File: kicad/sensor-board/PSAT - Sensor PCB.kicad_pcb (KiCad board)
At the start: 2 copper layers, 120 x 120 mm, 16 parts, among them J1 MCU Conn_01x04, J2 Conn_01x02, J3 Conn_01x03, J4 Conn_01x03, J5 Conn_01x01, U1 MPU-6000, U2 BME280

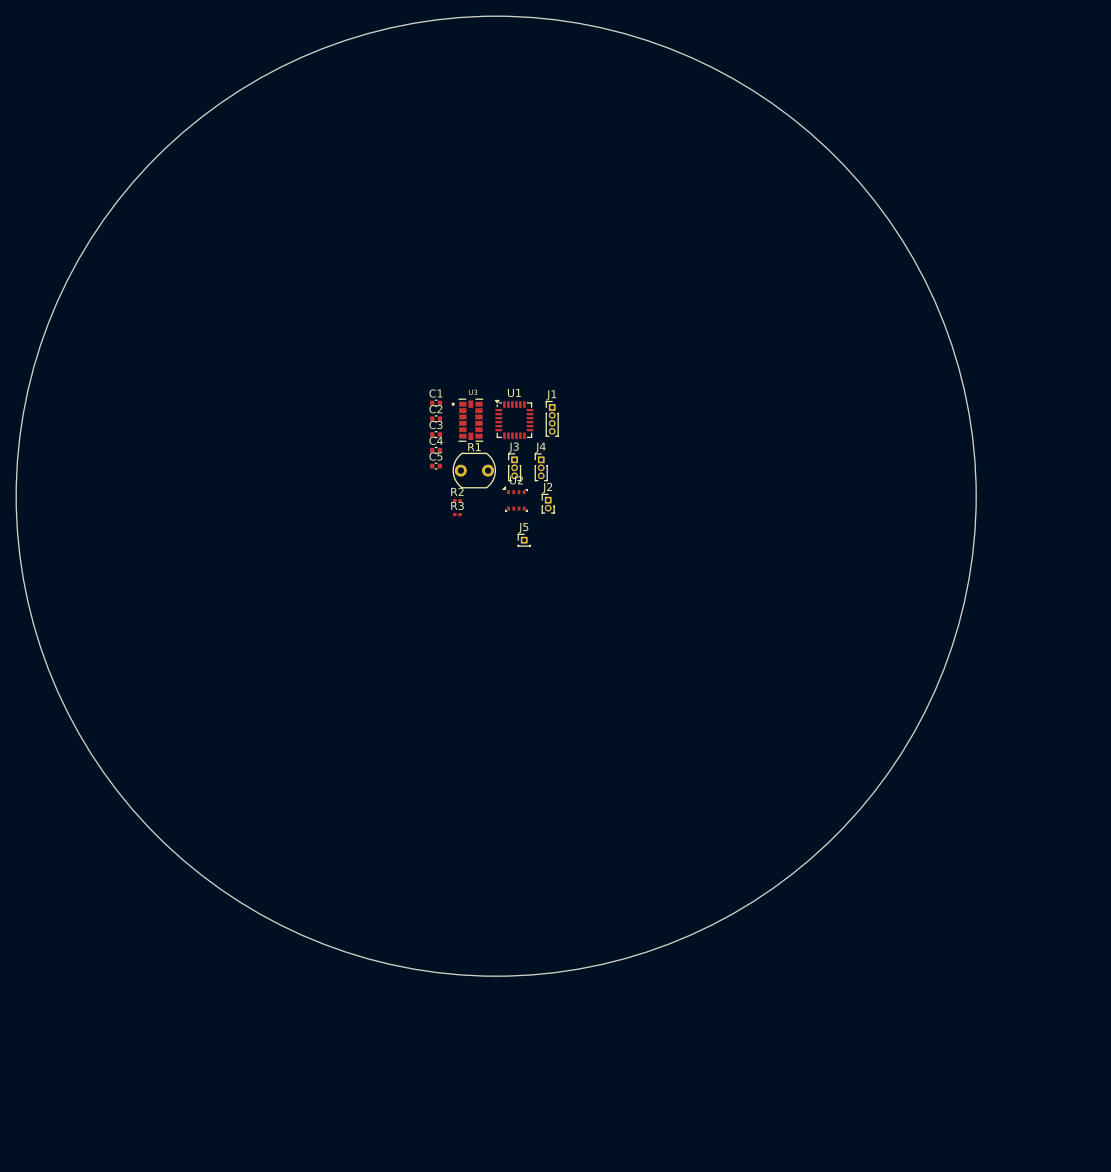
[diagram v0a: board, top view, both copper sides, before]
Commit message: feat: sensor board schematic and started pcb
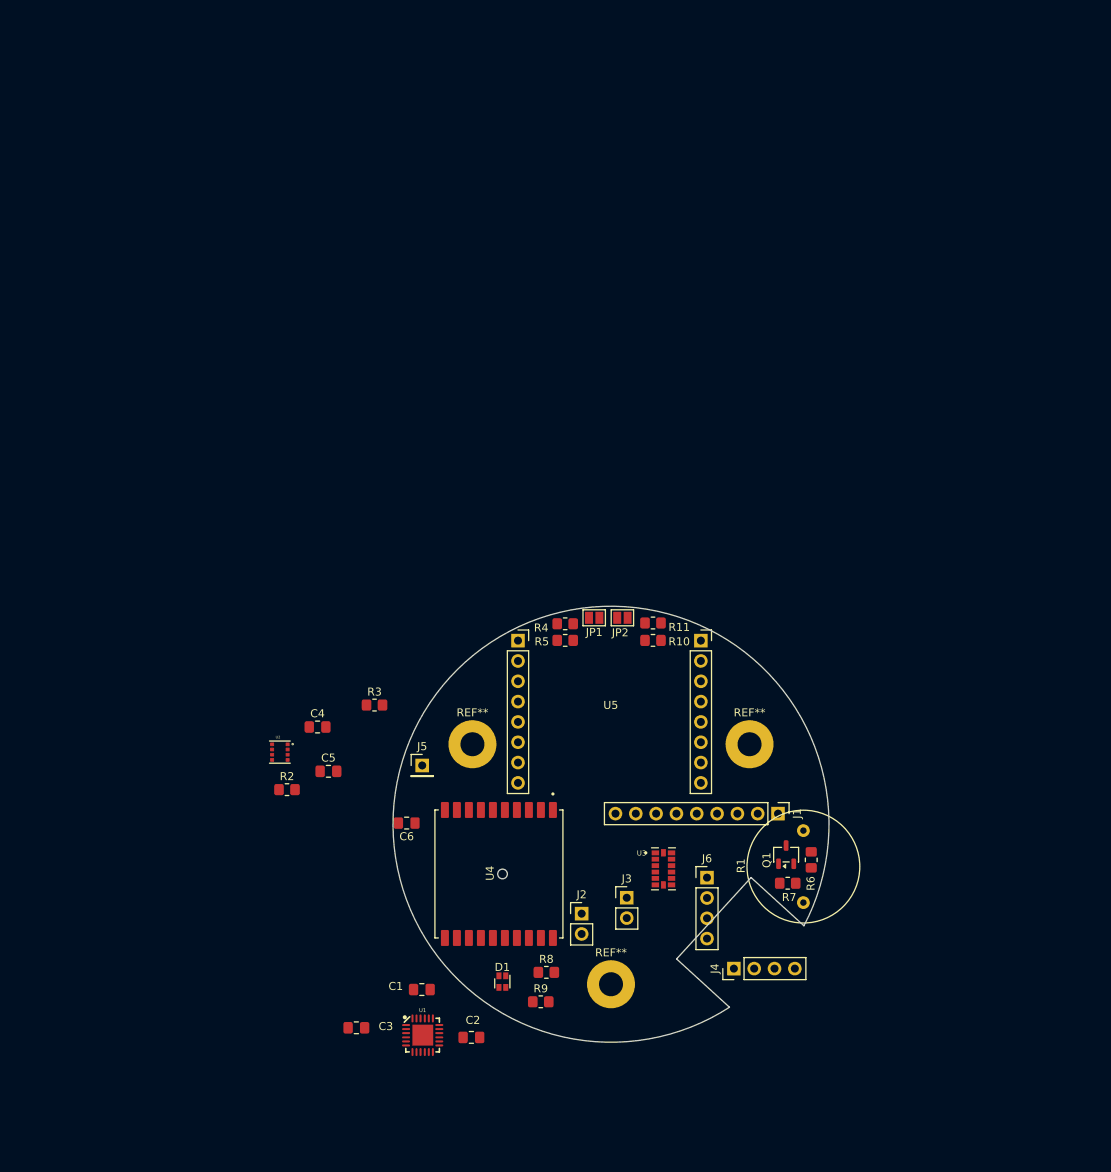
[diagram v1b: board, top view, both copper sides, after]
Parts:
- added C6: 22uF, Capacitor_SMD:C_0805_2012Metric_Pad1.18x1.45mm_HandSolder, F.Cu at (92.3, 140.4)
- added D1: LED, LED_SMD:LED_LiteOn_LTST-C19HE1WT, F.Cu at (104.3, 160.2)
- added J6: MCU - Conn_01x04, Connector_PinHeader_2.54mm:PinHeader_1x04_P2.54mm_Vertical, F.Cu at (129.8, 147.2)
- added JP1: EN_5, Jumper:SolderJumper-2_P1.3mm_Open_Pad1.0x1.5mm, F.Cu at (115.8, 114.7)
- added JP2: EN_5, Jumper:SolderJumper-2_P1.3mm_Open_Pad1.0x1.5mm, F.Cu at (119.3, 114.7)
- added Q1: Q_NPN_BCE, Package_TO_SOT_SMD:SOT-23-3, F.Cu at (139.7, 144.3)
- added R10: 1k5, Resistor_SMD:R_0805_2012Metric_Pad1.20x1.40mm_HandSolder, F.Cu at (123.1, 117.5)
- added R11: 1Meg, Resistor_SMD:R_0805_2012Metric_Pad1.20x1.40mm_HandSolder, F.Cu at (123.1, 115.3)
- added R4: 1k5, Resistor_SMD:R_0805_2012Metric_Pad1.20x1.40mm_HandSolder, F.Cu at (112.1, 115.5)
- added R5: 1Meg, Resistor_SMD:R_0805_2012Metric_Pad1.20x1.40mm_HandSolder, F.Cu at (112.1, 117.5)
- added R6: 10k, Resistor_SMD:R_0805_2012Metric_Pad1.20x1.40mm_HandSolder, F.Cu at (142.9, 145.0)
- added R7: 10k, Resistor_SMD:R_0805_2012Metric_Pad1.20x1.40mm_HandSolder, F.Cu at (139.9, 147.9)
- added R8: 1k, Resistor_SMD:R_0805_2012Metric_Pad1.20x1.40mm_HandSolder, F.Cu at (109.8, 159.0)
- added R9: 180k, Resistor_SMD:R_0805_2012Metric_Pad1.20x1.40mm_HandSolder, F.Cu at (109.1, 162.7)
- added REF**: MountingHole_3mm_Pad, MountingHole:MountingHole_3mm_Pad, F.Cu at (100.5, 130.5)
- added REF**: MountingHole_3mm_Pad, MountingHole:MountingHole_3mm_Pad, F.Cu at (117.9, 160.5)
- added REF**: MountingHole_3mm_Pad, MountingHole:MountingHole_3mm_Pad, F.Cu at (135.2, 130.5)
- added U4: CD-PA1616D, gps:XCVR_CD-PA1616D, F.Cu at (103.8, 146.7)
- added U5: ESP32-CAM, Connector_PinSocket_2.54mm:ESPCam, F.Cu at (117.8, 126.1)
- C1, C2, C3, C4, C5: footprint Capacitor_SMD:C_0402_1005Metric -> Capacitor_SMD:C_0805_2012Metric_Pad1.18x1.45mm_HandSolder
- J1: value MCU Conn_01x04 -> Conn_01x09_Pin; footprint Connector_PinHeader_1.00mm:PinHeader_1x04_P1.00mm_Vertical -> Connector_PinHeader_2.54mm:PinHeader_1x09_P2.54mm_Vertical
- J2: footprint Connector_PinHeader_1.00mm:PinHeader_1x02_P1.00mm_Vertical -> Connector_PinHeader_2.54mm:PinHeader_1x02_P2.54mm_Vertical
- J3: value Conn_01x03 -> MCU - Conn_01x02; footprint Connector_PinHeader_1.00mm:PinHeader_1x03_P1.00mm_Vertical -> Connector_PinHeader_2.54mm:PinHeader_1x02_P2.54mm_Vertical
- J4: value Conn_01x03 -> MCU - Conn_01x04; footprint Connector_PinHeader_1.00mm:PinHeader_1x03_P1.00mm_Vertical -> Connector_PinHeader_2.54mm:PinHeader_1x04_P2.54mm_Vertical
- J5: footprint Connector_PinHeader_1.00mm:PinHeader_1x01_P1.00mm_Vertical -> Connector_PinHeader_2.54mm:PinHeader_1x01_P2.54mm_Vertical
- R1: footprint OptoDevice:R_LDR_5.1x4.3mm_P3.4mm_Vertical -> OptoDevice:R_LDR_D13.8mm_P9.0mm_Vertical
- R2, R3: footprint Resistor_SMD:R_0201_0603Metric -> Resistor_SMD:R_0805_2012Metric_Pad1.20x1.40mm_HandSolder
- U1: footprint Sensor_Motion:InvenSense_QFN-24_4x4mm_P0.5mm -> mpu6000:QFN-24-EP
- U2: footprint Package_LGA:Bosch_LGA-8_2.5x2.5mm_P0.65mm_ClockwisePinNumbering -> bme280:PSON65P250X250X100-8N
- U3: value ~ -> ADXL375; footprint ADXL375BCCZ-RL7 (1):PQFN80P500X300X100-14N -> ADXL375:PQFN80P500X300X100-14N
- moved U1 77.7 mm to (94.3, 166.9)
- moved C2 77.4 mm to (100.4, 167.2)
- moved C3 74.8 mm to (86.0, 165.9), turned to 180 degrees
- moved C1 73.3 mm to (94.2, 161.2)
- moved R1 68.9 mm to (141.9, 150.3), turned to 90 degrees
- moved J4 68.0 mm to (133.2, 158.6), turned to 90 degrees
- moved U3 61.0 mm to (124.4, 146.1)
- moved J1 58.1 mm to (138.7, 139.2), turned to -90 degrees
- moved J3 56.5 mm to (119.8, 149.7)
- moved J2 51.8 mm to (114.2, 151.7)
- moved U2 43.2 mm to (76.5, 131.5)
- moved R2 41.9 mm to (77.3, 136.2)
- moved C5 40.5 mm to (82.5, 133.9)
- moved C4 37.6 mm to (81.2, 128.3)
- moved J5 30.9 mm to (94.2, 133.2)
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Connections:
- C2 pad 1: +3.3V -> SDA
- C4 pad 1: +3.3V -> SDA
- C5 pad 1: Net-(J2-Pin_1) -> SDA
- J1 pad 1: Net-(J1-Pin_1) -> D-
- J1 pad 2: Net-(J1-Pin_2) -> D+
- J1 pad 3: Net-(J1-Pin_3) -> unconnected-(J1-Pin_3-Pad3)
- J1 pad 4: Net-(J1-Pin_4) -> PG_3.3
- J2 pad 1: Net-(J2-Pin_1) -> GPS_UART_TX
- J2 pad 2: Net-(J2-Pin_1) -> GPS_UART_RX
- J4 pad 1: Net-(J4-Pin_1) -> ADO
- J4 pad 2: Net-(J4-Pin_2) -> SCL
- J4 pad 3: Net-(J4-Pin_3) -> SDA
- J5 pad 1: GND -> Net-(J5-Pin_1)
- R1 pad 1: +3.3V -> SDA
- R1 pad 2: GND -> Net-(Q1-B)
- R2 pad 1: Net-(J2-Pin_1) -> SDA
- R3 pad 1: Net-(J2-Pin_1) -> SDA
- U1 pad 12: Net-(J1-Pin_4) -> INT
- U1 pad 13: +3.3V -> SDA
- U1 pad 23: Net-(J1-Pin_1) -> SCL
- U1 pad 24: Net-(J1-Pin_3) -> SDA
- U1 pad 8: +3.3V -> unconnected-(U1-~{CS}-Pad8)
- U1 pad 9: Net-(J1-Pin_2) -> ADO
- U2 pad 3: Net-(J2-Pin_1) -> SDA
- U2 pad 4: Net-(J2-Pin_1) -> SCL
- U2 pad 5: GND -> SDO
- U2 pad 6: Net-(J2-Pin_1) -> SDA
- U2 pad 8: +3.3V -> SDA
- U3 pad 1: unconnected-(U3-VDD_I/o-Pad1) -> SDA
- U3 pad 10: Net-(J3-Pin_3) -> unconnected-(U3-NC-Pad10)
- U3 pad 12: GND -> SDO_ACC
- U3 pad 13: Net-(J4-Pin_2) -> SDA
- U3 pad 14: Net-(J4-Pin_1) -> SCL
- U3 pad 3: +3.3V -> SDA
- U3 pad 6: +3.3V -> SDA
- U3 pad 7: Net-(J4-Pin_3) -> unconnected-(U3-CS-Pad7)
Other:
- board size 120 x 120 mm -> 54.5 x 54.5 mm

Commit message: feat: sensor board pcb
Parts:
- removed J5: Conn_01x01, Connector_PinHeader_2.54mm:PinHeader_1x01_P2.54mm_Vertical
- removed REF** (x3): MountingHole_3mm_Pad, MountingHole:MountingHole_3mm_Pad
- added H1: MountingHole, MountingHole:MountingHole_3mm_Pad, F.Cu at (100.5, 130.5)
- added H2: MountingHole, MountingHole:MountingHole_3mm_Pad, F.Cu at (135.2, 130.5)
- added H3: MountingHole, MountingHole:MountingHole_3mm_Pad, F.Cu at (117.9, 160.5)
- added JP3: EN_5, Jumper:SolderJumper-2_P1.3mm_Open_Pad1.0x1.5mm, F.Cu at (137.5, 125.7)
- added JP4: EN_5, Jumper:SolderJumper-2_P1.3mm_Open_Pad1.0x1.5mm, F.Cu at (103.5, 120.0)
- D1: footprint LED_SMD:LED_LiteOn_LTST-C19HE1WT -> LED_SMD:LED_0805_2012Metric
- J1: value Conn_01x09_Pin -> Conn_01x06; footprint Connector_PinHeader_2.54mm:PinHeader_1x09_P2.54mm_Vertical -> Connector_PinHeader_2.54mm:PinHeader_1x06_P2.54mm_Vertical
- J3: value MCU - Conn_01x02 -> Conn_01x03_Pin; footprint Connector_PinHeader_2.54mm:PinHeader_1x02_P2.54mm_Vertical -> Connector_PinHeader_2.54mm:PinHeader_1x03_P2.54mm_Vertical
- J4: value MCU - Conn_01x04 -> Conn_01x03; footprint Connector_PinHeader_2.54mm:PinHeader_1x04_P2.54mm_Vertical -> Connector_PinHeader_2.54mm:PinHeader_1x03_P2.54mm_Vertical
- moved C3 53.9 mm to (118.5, 123.0), turned to 90 degrees
- moved U1 52.8 mm to (122.6, 122.3), turned to -90 degrees
- moved C1 45.8 mm to (123.4, 126.0)
- moved C2 44.6 mm to (117.5, 126.0), turned to 180 degrees
- moved U2 38.2 mm to (113.0, 120.5)
- moved J6 36.8 mm to (94.0, 139.0), turned to 180 degrees
- moved R2 36.0 mm to (111.0, 123.5)
- moved C5 32.9 mm to (114.0, 124.6), turned to -90 degrees
- moved J1 31.5 mm to (113.1, 157.5)
- moved C4 29.9 mm to (110.0, 120.5), turned to 90 degrees
- moved J3 27.7 mm to (132.5, 125.0), turned to 180 degrees
- moved R9 23.5 mm to (96.3, 142.9)
- moved R3 22.7 mm to (111.0, 125.5)
- moved R8 19.0 mm to (96.2, 145.8), turned to 180 degrees
- moved J2 18.1 mm to (96.2, 150.7)
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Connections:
- C2 pad 1: SDA -> 3.3V
- C4 pad 1: SDA -> 3.3V
- C5 pad 1: SDA -> 3.3V
- C6 pad 1: GPS 3V3 -> 3.3V
- J1 pad 1: D- -> ADO
- J1 pad 2: D+ -> LIGHT
- J1 pad 3: unconnected-(J1-Pin_3-Pad3) -> SCL2
- J1 pad 4: PG_3.3 -> SCL1
- J1 pad 5: PG_1.8 -> SDA2
- J1 pad 6: GND -> SDA1
- J3 pad 1: Net-(J3-Pin_1) -> 3.3V
- J3 pad 2: Net-(J3-Pin_2) -> 5V
- J4 pad 1: ADO -> INT
- J4 pad 2: SCL -> Net-(J4-Pin_2)
- J4 pad 3: SDA -> Net-(J4-Pin_3)
- Q1 pad 2: Net-(J5-Pin_1) -> LIGHT
- R1 pad 1: SDA -> 3.3V
- R2 pad 1: SDA -> SDA1
- R3 pad 1: SDA -> 3.3V
- R7 pad 1: Net-(J5-Pin_1) -> LIGHT
- R7 pad 2: SDA -> 3.3V
- R9 pad 1: GPS 3V3 -> 3.3V
- U1 pad 13: SDA -> 3.3V
- U1 pad 23: SCL -> SCL2
- U1 pad 24: SDA -> SDA2
- U2 pad 3: SDA -> SDA1
- U2 pad 4: SCL -> SCL1
- U2 pad 5: SDO -> SDO_PRESSURE
- U2 pad 6: SDA -> 3.3V
- U2 pad 8: SDA -> 3.3V
- U3 pad 1: SDA -> 3.3V
- U3 pad 13: SDA -> SDA1
- U3 pad 14: SCL -> SCL1
- U3 pad 3: SDA -> 3.3V
- U3 pad 6: SDA -> 3.3V
- U3 pad 8: Net-(J3-Pin_1) -> Net-(J4-Pin_2)
- U3 pad 9: Net-(J3-Pin_2) -> Net-(J4-Pin_3)
- U4 pad 1: GPS 3V3 -> 3.3V
- U4 pad 14: SCL -> SCL2
- U4 pad 15: SDA -> SDA2
- U5 pad 1: +5V -> Net-(JP4-B)
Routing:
- net 3.3V: track 0.00 -> 125.3 mm, vias 0 -> 10
- net SDA1: track 0.00 -> 71.2 mm, vias 0 -> 2
- net SCL1: track 0.00 -> 55.7 mm, vias 0 -> 6
- net SDA2: track 0.00 -> 54.3 mm, vias 0 -> 4
- net SCL2: track 0.00 -> 48.6 mm, vias 0 -> 6
- net ADO: track 0.00 -> 48.3 mm, vias 0 -> 4
- net INT: track 0.00 -> 41.6 mm, vias 0 -> 6
- net LIGHT: track 0.00 -> 39.1 mm, vias 0 -> 2
- net GND: track 0.00 -> 36.6 mm, vias 0 -> 27
- net 5V: track 0.00 -> 34.0 mm, vias 0 -> 1
- net Net-(J4-Pin_3): track 0.00 -> 30.6 mm, vias 0 -> 2
- net Net-(J4-Pin_2): track 0.00 -> 28.6 mm, vias 0 -> 2
- net SDO_ACC: track 0.00 -> 18.1 mm, vias 0 -> 2
- net Net-(J6-Pin_3): track 0.00 -> 16.1 mm
- net Net-(JP3-B): track 0.00 -> 16.0 mm
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- added copper zone on B.Cu, net GND
- added copper zone on F.Cu, net GND
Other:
- board text added: "3.3V"
- board text added: "5V"
- board text added: "ACC"
- board text added: "AD0"
- board text added: "Dear PSAT Team, We couldnt figure out soldermask expansion errors pls help :)"
- board text added: "GND"
- board text added: "GPS Sensor"
- board text added: "High G"
- board text added: "INT"
- board text added: "INT1"
- board text added: "INT2"
- board text added: "IO12"
- board text added: "IO13"
- board text added: "IO14"
- board text added: "IO15"
- board text added: "LIGHT"
- board text added: "Light Sensor"
- board text added: "Low G"
- board text added: "PRE"
- board text added: "Pressure"
- board text added: "RX"
- board text added: "SCL1"
- board text added: "SCL2"
- board text added: "SDA1"
- board text added: "SDA2"
- board text added: "TX"
- board text added: "never gonna give you up"
